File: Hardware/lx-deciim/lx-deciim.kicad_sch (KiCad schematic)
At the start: 2 parts

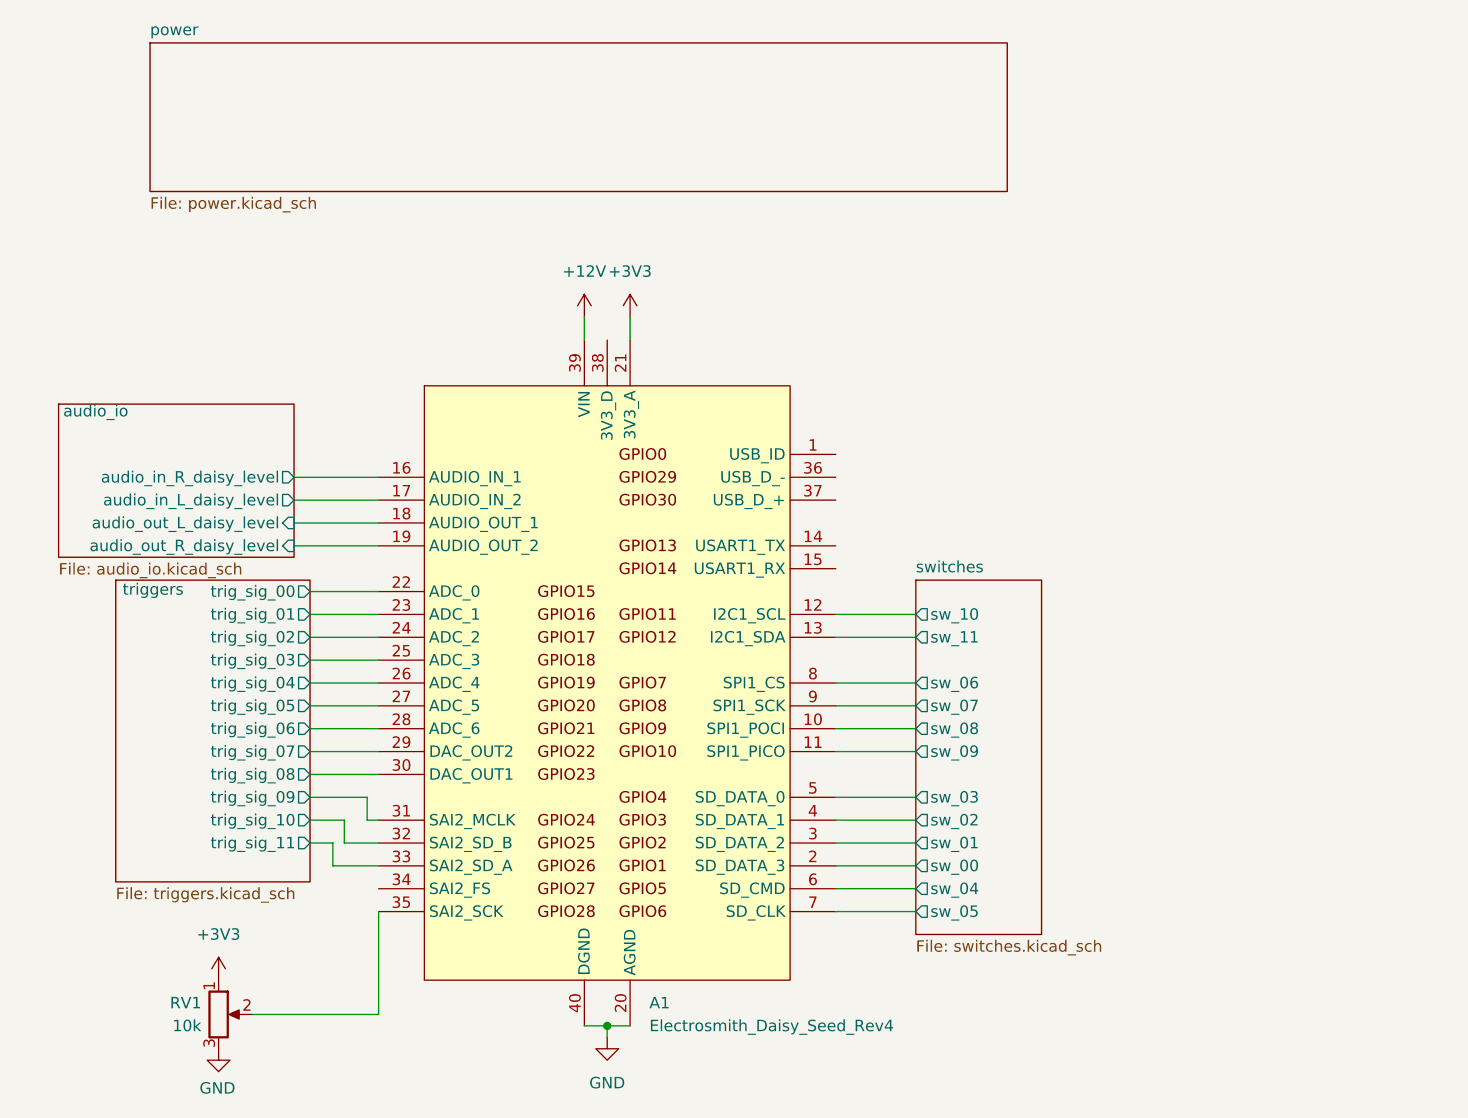
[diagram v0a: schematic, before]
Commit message: feature: first draft routing
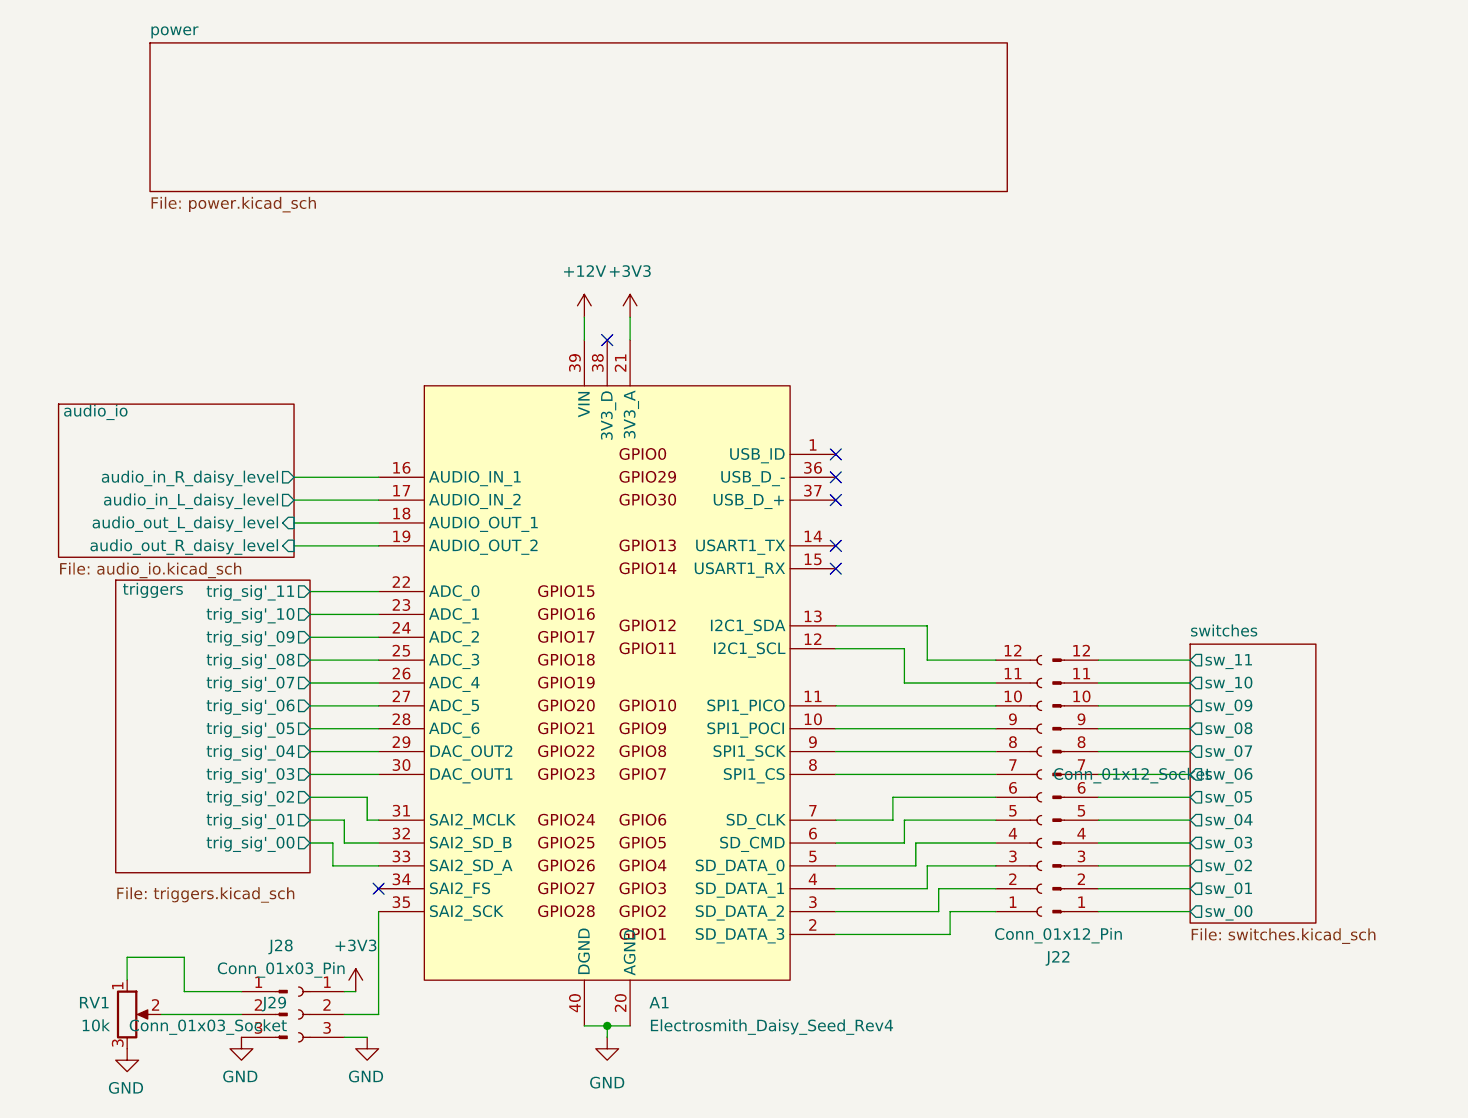
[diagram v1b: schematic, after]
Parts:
- added J22: Conn_01x12_Pin, Connector_PinHeader_2.54mm:PinHeader_1x12_P2.54mm_Vertical, symbol Connector:Conn_01x12_Pin
- added J23: Conn_01x12_Socket, Connector_PinSocket_2.54mm:PinSocket_1x12_P2.54mm_Vertical, symbol Connector:Conn_01x12_Socket
- added J28: Conn_01x03_Pin, Connector_PinHeader_2.54mm:PinHeader_1x03_P2.54mm_Vertical, symbol Connector:Conn_01x03_Pin
- added J29: Conn_01x03_Socket, Connector_PinSocket_2.54mm:PinSocket_1x03_P2.54mm_Vertical, symbol Connector:Conn_01x03_Socket
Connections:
- net +3V3: now also J29.1 (Pin_1); no longer RV1.1
- net GND: now also J28.3 (Pin_3), J29.3 (Pin_3)
- net switches/sw_00: now also J22.1 (Pin_1); no longer A1.2 (SD_DATA_3)
- net switches/sw_01: now also J22.2 (Pin_2); no longer A1.3 (SD_DATA_2)
- net switches/sw_02: now also J22.3 (Pin_3); no longer A1.4 (SD_DATA_1)
- net switches/sw_03: now also J22.4 (Pin_4); no longer A1.5 (SD_DATA_0)
- net switches/sw_04: now also J22.5 (Pin_5); no longer A1.6 (SD_CMD)
- net switches/sw_05: now also J22.6 (Pin_6); no longer A1.7 (SD_CLK)
- net switches/sw_06: now also J22.7 (Pin_7); no longer A1.8 (SPI1_CS)
- net switches/sw_07: now also J22.8 (Pin_8); no longer A1.9 (SPI1_SCK)
- net switches/sw_08: now also J22.9 (Pin_9); no longer A1.10 (SPI1_POCI)
- net switches/sw_09: now also J22.10 (Pin_10); no longer A1.11 (SPI1_PICO)
- net switches/sw_10: now also J22.11 (Pin_11); no longer A1.12 (I2C1_SCL)
- net switches/sw_11: now also J22.12 (Pin_12); no longer A1.13 (I2C1_SDA)
- net at RV1.2: now also J28.2 (Pin_2); no longer A1.35 (SAI2_SCK)
- net triggers/trig_sig_00 renamed triggers/trig_sig'_11
- net triggers/trig_sig_01 renamed triggers/trig_sig'_10
- net triggers/trig_sig_02 renamed triggers/trig_sig'_09
- net triggers/trig_sig_03 renamed triggers/trig_sig'_08
- net triggers/trig_sig_04 renamed triggers/trig_sig'_07
- net triggers/trig_sig_05 renamed triggers/trig_sig'_06
- net triggers/trig_sig_06 renamed triggers/trig_sig'_05
- net triggers/trig_sig_07 renamed triggers/trig_sig'_04
- net triggers/trig_sig_08 renamed triggers/trig_sig'_03
- net triggers/trig_sig_09 renamed triggers/trig_sig'_02
- net triggers/trig_sig_10 renamed triggers/trig_sig'_01
- net triggers/trig_sig_11 renamed triggers/trig_sig'_00
- new net: A1.2 (SD_DATA_3), J23.1 (Pin_1)
- new net: A1.11 (SPI1_PICO), J23.10 (Pin_10)
- new net: A1.12 (I2C1_SCL), J23.11 (Pin_11)
- new net: A1.13 (I2C1_SDA), J23.12 (Pin_12)
- new net: A1.3 (SD_DATA_2), J23.2 (Pin_2)
- new net: A1.4 (SD_DATA_1), J23.3 (Pin_3)
- new net: A1.5 (SD_DATA_0), J23.4 (Pin_4)
- new net: A1.6 (SD_CMD), J23.5 (Pin_5)
- new net: A1.7 (SD_CLK), J23.6 (Pin_6)
- new net: A1.8 (SPI1_CS), J23.7 (Pin_7)
- new net: A1.9 (SPI1_SCK), J23.8 (Pin_8)
- new net: A1.10 (SPI1_POCI), J23.9 (Pin_9)
- new net: J28.1 (Pin_1), RV1.1
- new net: A1.35 (SAI2_SCK), J29.2 (Pin_2)
- no-connect marks 0 -> 7
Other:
- sheet triggers ports: added trig_sig'_00, trig_sig'_01, trig_sig'_02, trig_sig'_03, trig_sig'_04, trig_sig'_05, trig_sig'_06, trig_sig'_07, trig_sig'_08, trig_sig'_09, trig_sig'_10, trig_sig'_11; removed trig_sig_00, trig_sig_01, trig_sig_02, trig_sig_03, trig_sig_04, trig_sig_05, trig_sig_06, trig_sig_07, trig_sig_08, trig_sig_09, trig_sig_10, trig_sig_11
- moved on the sheet: RV1

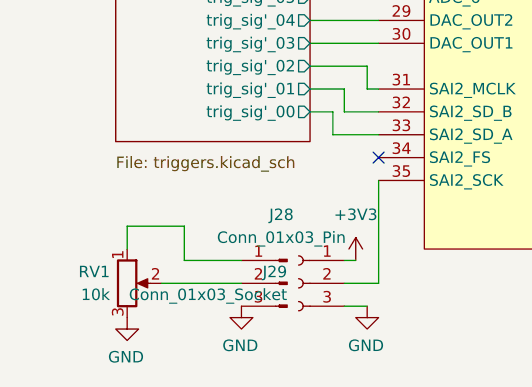
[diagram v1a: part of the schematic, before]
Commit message: feature: prep files for export (fill bom, gerber)
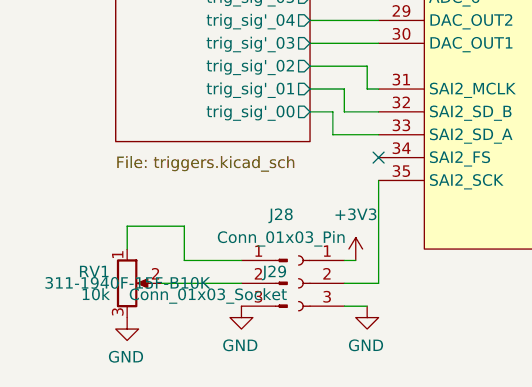
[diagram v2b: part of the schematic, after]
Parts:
- RV1: Mouser Part Number (none) -> 311-1940F-15F-B10K
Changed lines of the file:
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@@
+			)
+		)
+		(property "Mouser Part Number" "311-1940F-15F-B10K"
+			(at 85.09 148.59 0)
+			(effects
+				(font
+					(size 1.27 1.27)
+				)
 			)
 		)

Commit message: fix: fix mouser part number on schematic + fill page settings
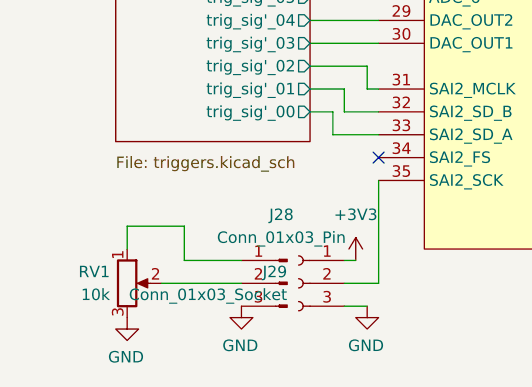
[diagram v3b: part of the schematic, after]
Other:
- company: (none) -> Lucas Bonvin
- title: (none) -> lx-deciim
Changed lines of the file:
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@@
 	(generator_version "9.0")
 	(paper "A4")
+	(title_block
+		(title "lx-deciim")
+		(date "2025-06-17")
+		(rev "v1.0.0")
+		(company "Lucas Bonvin")
+		(comment 1 "This project is licensed under the CC BY-NC 4.0 License.")
+	)
 	(junction
 		(at 138.43 149.86)
@@
 					(size 1.27 1.27)
 				)
-			)
-		)
+				(hide yes)
+			)
+		)
